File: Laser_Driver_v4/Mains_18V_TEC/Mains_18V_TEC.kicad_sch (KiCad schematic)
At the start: 92 parts, among them J1 Screw_Terminal_01x03, J2 Screw_Terminal_01x03, J3 Screw_Terminal_01x03, J4 Screw_Terminal_01x03, J5 Screw_Terminal_01x03, J6 DIN41612_M_3x8+8_Power_Male, Q1 IRF540NPBF, Q10 Q_NPN MJL21194, Q2 IRF9540NPBF, Q3 IRF540NPBF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

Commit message: Corrected card dimension now need to replace
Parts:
- removed H1, H2, H3, H4: MountingHole_Pad, MountingHole:MountingHole_3.2mm_M3, symbol Mechanical:MountingHole_Pad
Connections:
- net +22V: now also J6.P5
- net +6V_TEC: now also J6.P1
- net -22V: now also J6.P7
- net -6V_TEC: now also J6.P3
- net DGND: now also J6.P2, J6.P4
- no-connect marks 0 -> 24

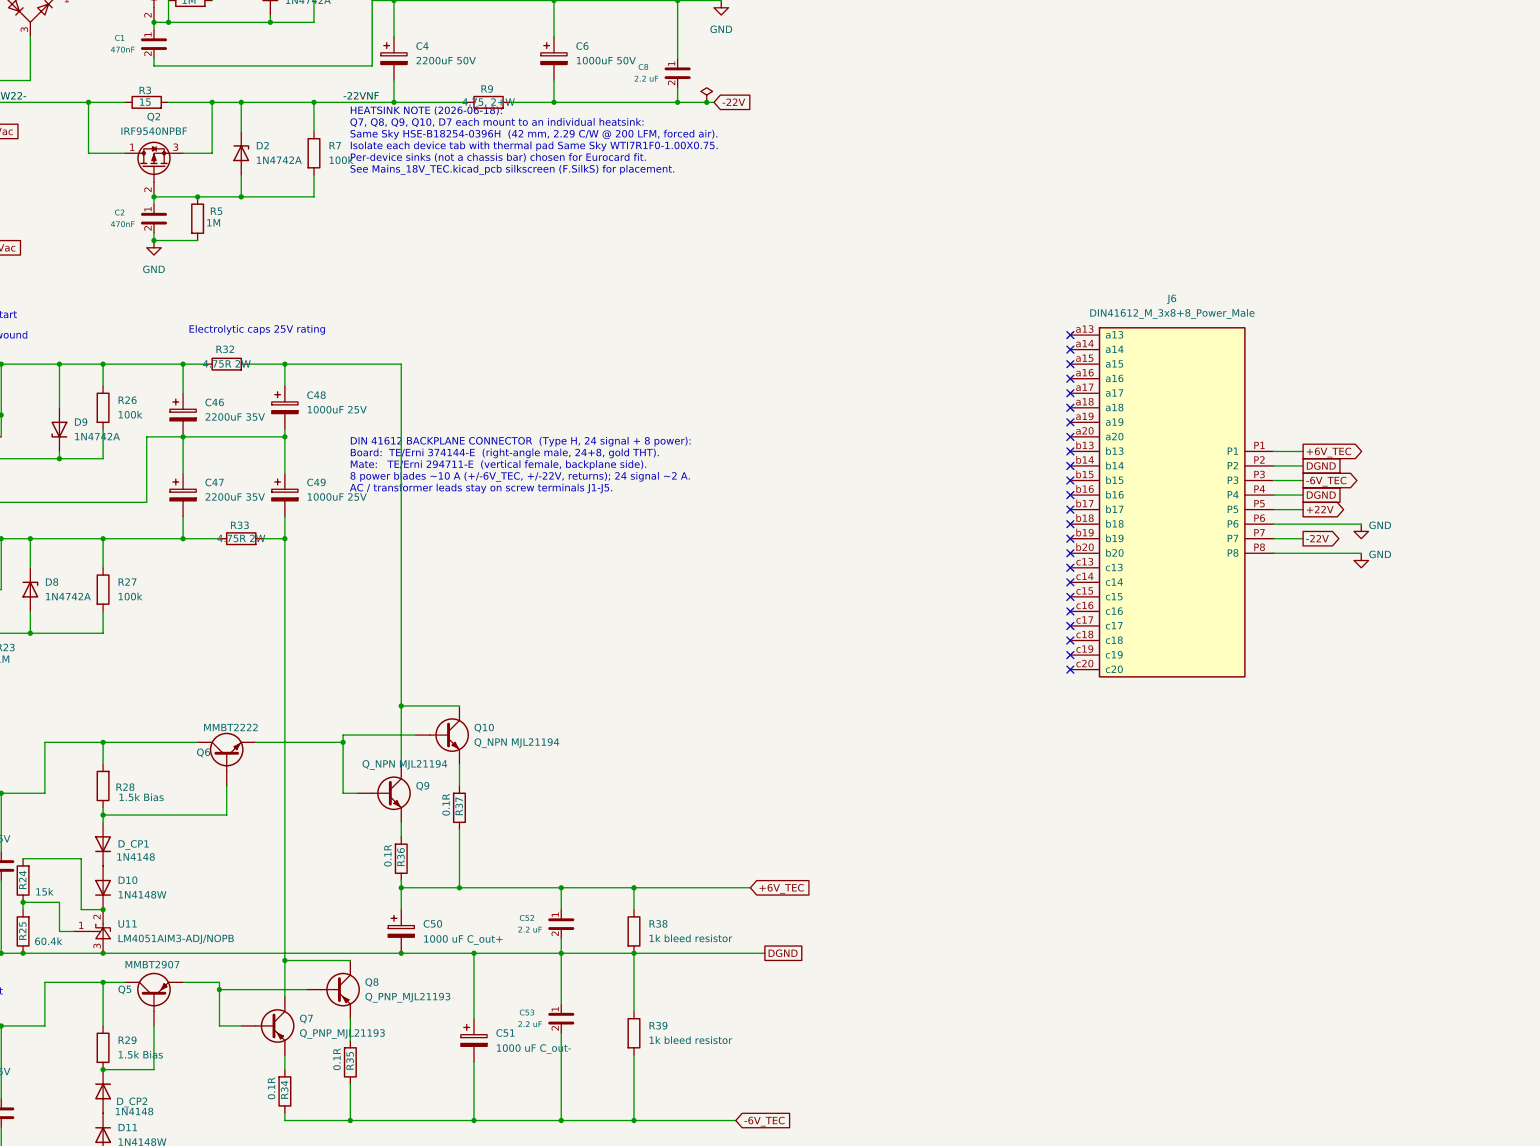
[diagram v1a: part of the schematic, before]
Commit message: version 5 further split power 22 V and 6 V 2-pcbs
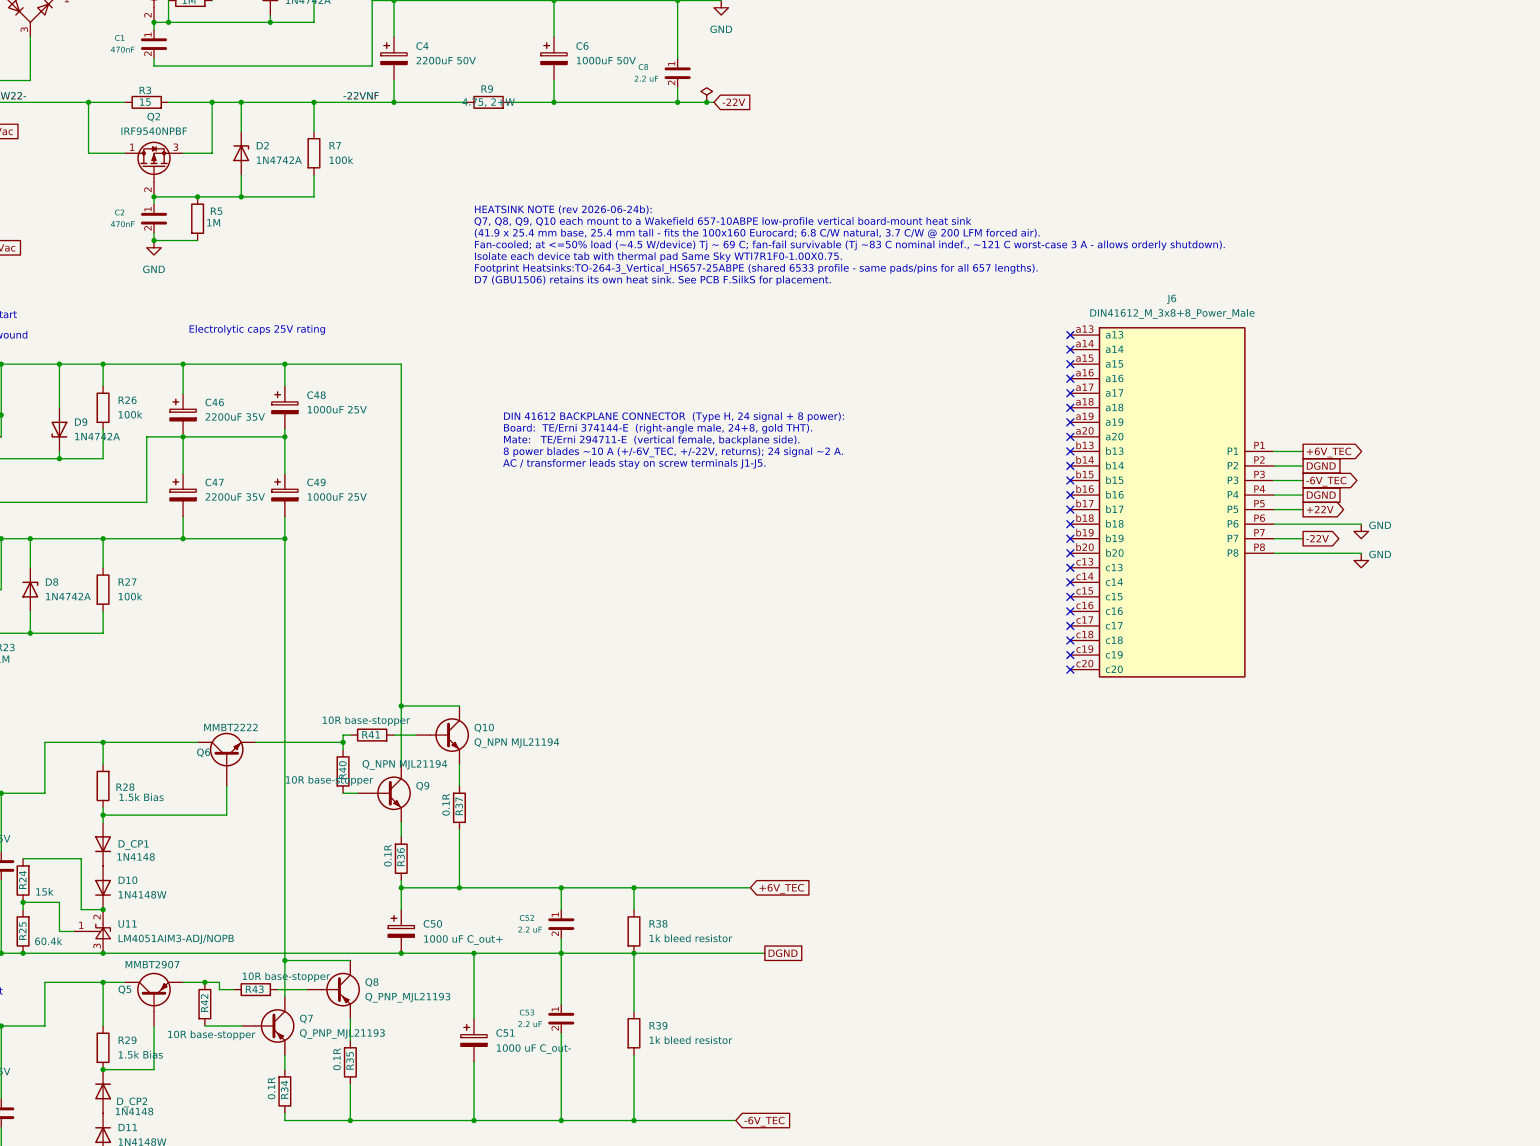
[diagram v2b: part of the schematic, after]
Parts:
- removed R32, R33: 4.75R 2W, RCL12254R75FKEG:RESC3263X80N, symbol Device:R
- added R40, R41, R42, R43: 10R base-stopper, Resistor_SMD:R_0805_2012Metric_Pad1.20x1.40mm_HandSolder, symbol Device:R
- Q10, Q7, Q8, Q9: footprint Package_TO_SOT_THT:TO-264-3_Vertical -> Heatsinks:TO-264-3_Vertical_HS657-25ABPE
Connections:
- net at C49.2, Q7.2 (C), Q8.2 (C): now also C47.2, D8.1 (K), Q4.3 (S), R21.2, R27.1
- net at C48.1, Q10.2 (C), Q9.2 (C): now also C46.1, D9.2 (A), Q3.3 (S), R20.2, R22.2, R26.1
- new net: Q5.2 (E), R42.1, R43.1
- new net: Q8.1 (B), R43.2
- new net: Q9.1 (B), R40.2
- new net: Q7.1 (B), R42.2
- new net: Q6.2 (E), R40.1, R41.1
- new net: Q10.1 (B), R41.2
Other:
- note added: "HEATSINK NOTE (rev 2026-06-24b): Q7, Q8, Q9, Q10 each mount to a Wakefield 657-10ABPE low-profile vertical board-mount heat sink (41.9 x 25.4 mm base, 25.4 mm tall - fits the 100x160 Eurocard; 6.8 C/W natural, 3.7 C/W @ 200 LFM forced air). Fan-cooled; at <=50% load (~4.5 W/device) Tj ~ 69 C; fan-fail survivable (Tj ~83 C nominal indef., ~121 C worst-case 3 A - allows orderly shutdown). Isolate e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"
- note removed: "HEATSINK NOTE (2026-06-18): Q7, Q8, Q9, Q10, D7 each mount to an individual heatsink: Same Sky HSE-B18254-0396H (42 mm, 2.29 C/W @ 200 LFM, forced air). Isolate each device tab with thermal pad Same Sky WTI7R1F0-1.00X0.75. Per-device sinks (not a chassis bar) chosen for Eurocard fit. See Mains_18V_TEC.kicad_pcb silkscreen (F.SilkS) for placement."
